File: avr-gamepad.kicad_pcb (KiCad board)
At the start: 2 copper layers, 26.2 x 48.3 mm, 33 parts, among them J1 Conn_01x08, J2 Conn_01x01, P1 USB_C_Plug_USB2.0, SW10 Up, SW11 Down, SW12 Left, SW13 Select, SW2 R, SW3 X, SW4 A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

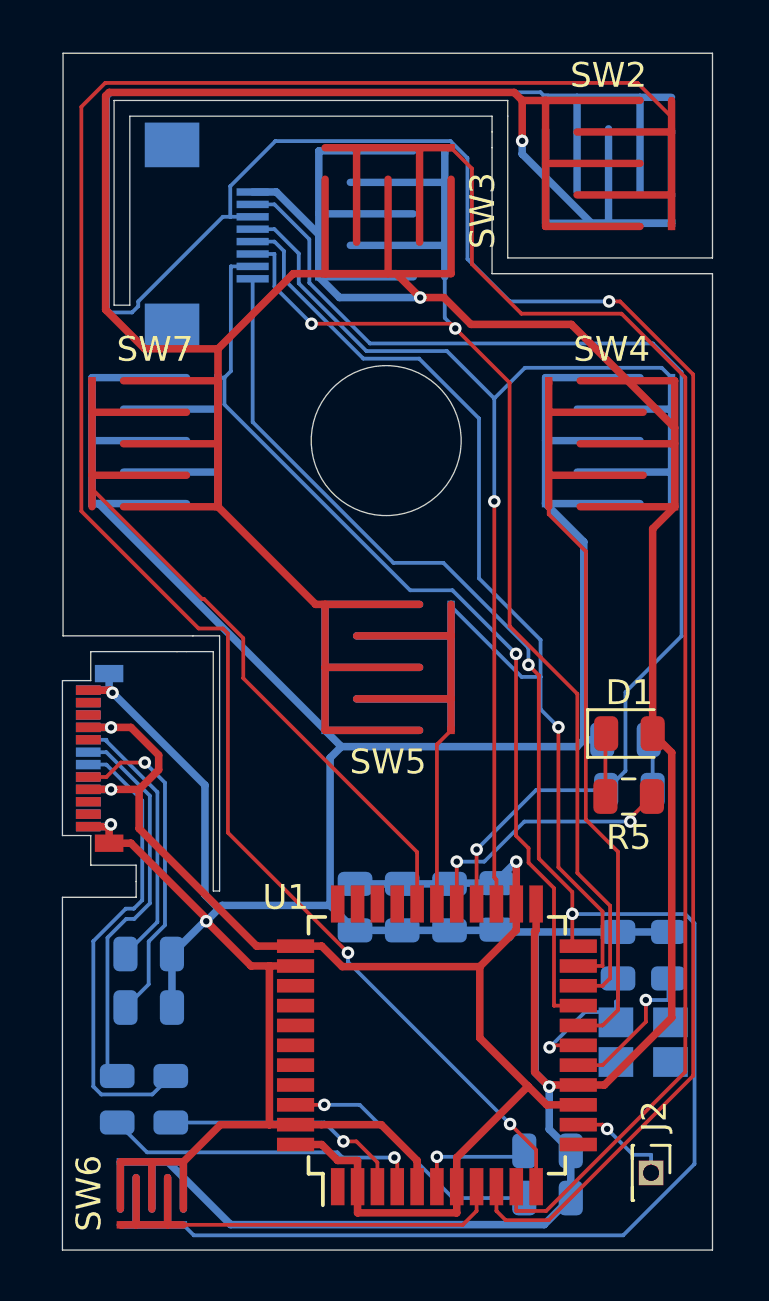
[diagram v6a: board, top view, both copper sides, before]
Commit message: move FFC back, improve routing
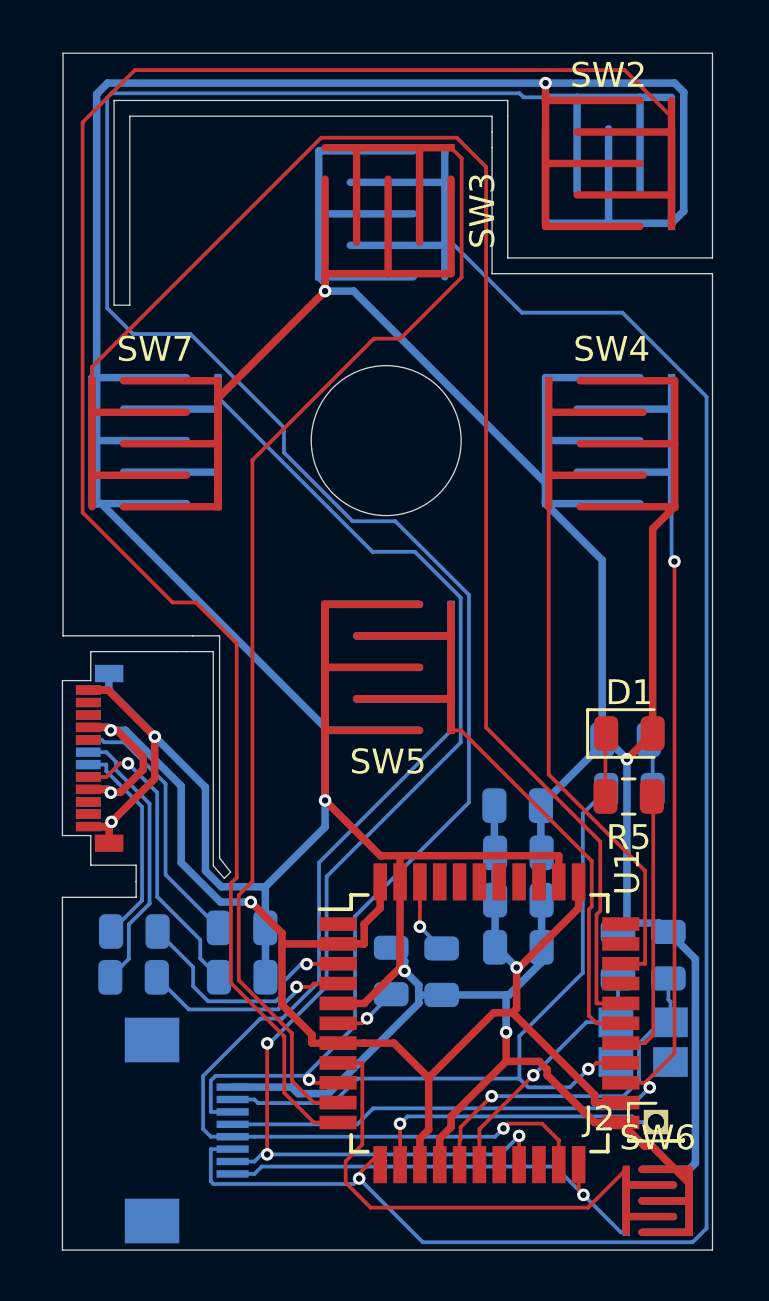
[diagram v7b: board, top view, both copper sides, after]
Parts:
- moved J1 36.1 mm to (132.5, 122.2)
- moved SW13 20.4 mm to (151.5, 125.0), turned to 180 degrees
- moved SW6 20.4 mm to (151.5, 125.0), turned to 180 degrees
- moved C7 10.1 mm to (142.7, 115.8), turned to 270 degrees
- moved C8 9.61 mm to (140.7, 115.7), turned to 90 degrees
- moved R4 6.92 mm to (130.4, 114.2), turned to 180 degrees
- moved C4 6.78 mm to (145.8, 114.8), turned to 0 degrees
- moved R2 4.96 mm to (130.3, 116.0), turned to 180 degrees
- moved C2 4.69 mm to (145.8, 112.9), turned to 0 degrees
- moved C3 4.15 mm to (145.8, 109.1), turned to 0 degrees
- moved R1 3.96 mm to (134.7, 116.0)
- moved R3 3.91 mm to (134.7, 114.0)
- moved C1 3.53 mm to (145.8, 111.0), turned to 0 degrees
- moved J2 2.06 mm to (151.4, 121.8), turned to 0 degrees
- moved U1 1.93 mm to (144.3, 117.9), turned to 0 degrees
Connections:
- J1 pad 3: /pd2 -> /pb7
- SW10 pad 1: /pd2 -> /pb7
- SW4 pad 1: /pd0 -> /pc6
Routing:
- net /pb7: track 0.00 -> 75.7 mm, vias 0 -> 1
- net /pd5: track 70.3 -> 18.4 mm, vias 2 -> 1
- net /pd2: track 47.7 -> 0.00 mm, vias 2 -> 0
- net /pb5: track 26.6 -> 57.4 mm
- net /pd0: track 28.4 -> 0.00 mm
- net GND: track 262.8 -> 234.9 mm, vias 6 -> 8
- net /pc6: track 0.00 -> 26.1 mm
- net /pb1: track 100.7 -> 75.9 mm
- net /pd6: track 47.7 -> 29.8 mm
- net /pd1: track 38.5 -> 52.8 mm, vias 1 -> 3
- net Net-(P1-PadA7): track 18.9 -> 8.57 mm
- net /pb2: track 53.7 -> 45.3 mm
- net /pb4: track 7.24 -> 15.5 mm
- net Net-(J2-Pad1): track 4.17 -> 12.2 mm
- net Net-(C7-Pad1): track 10.8 -> 3.05 mm
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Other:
- outline, holes or cut-outs redrawn

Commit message: rearrange, reroute, DRC fixes
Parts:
- moved J2 9.59 mm to (142.6, 125.8)
- moved R2 0.13 mm to (130.4, 116.1)
- moved R4 0.11 mm to (130.4, 114.0)
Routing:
- net Net-(J2-Pad1): track 12.2 -> 5.35 mm, vias 1 -> 2
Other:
- outline, holes or cut-outs redrawn
